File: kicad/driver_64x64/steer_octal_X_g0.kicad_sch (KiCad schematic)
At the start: 66 parts

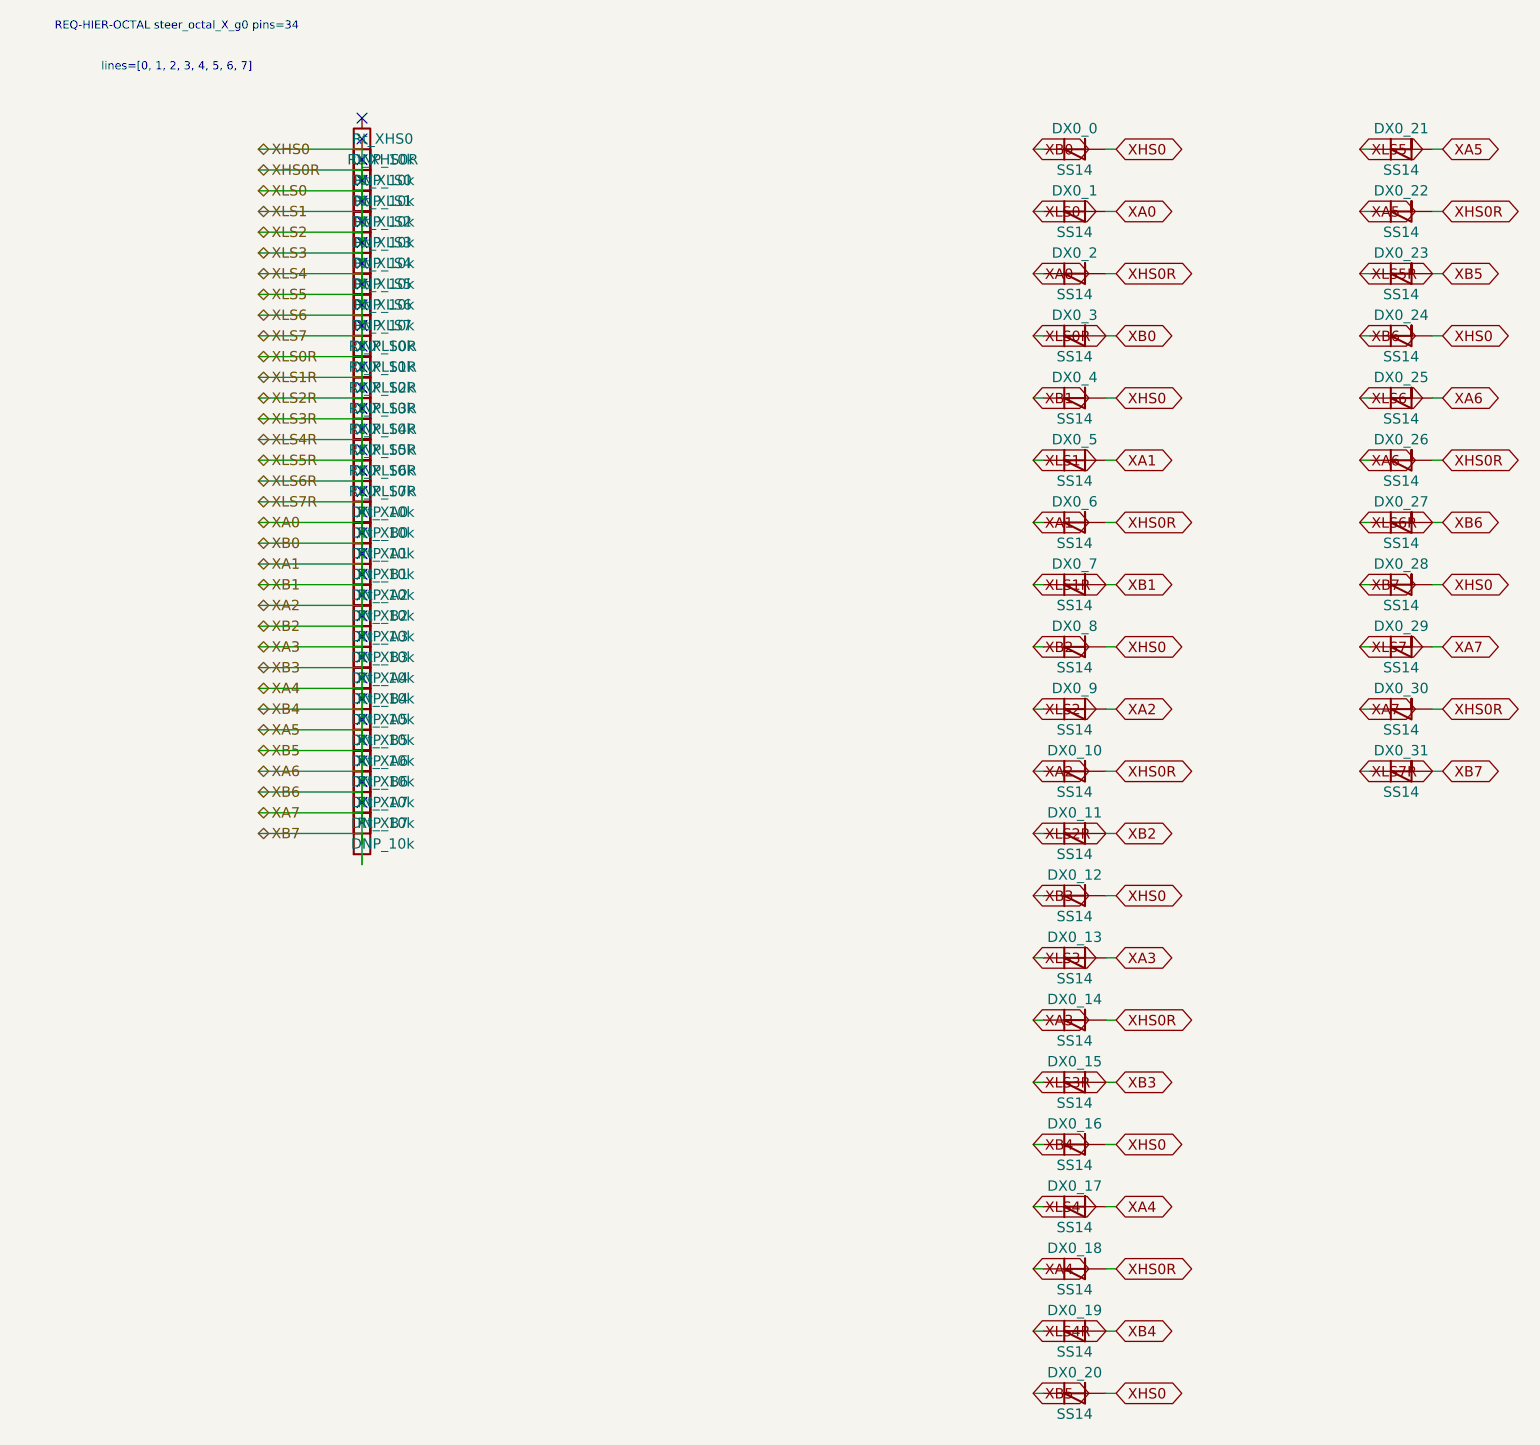
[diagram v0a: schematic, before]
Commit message: logical seperation into host and multiple decode/drive/steering boards
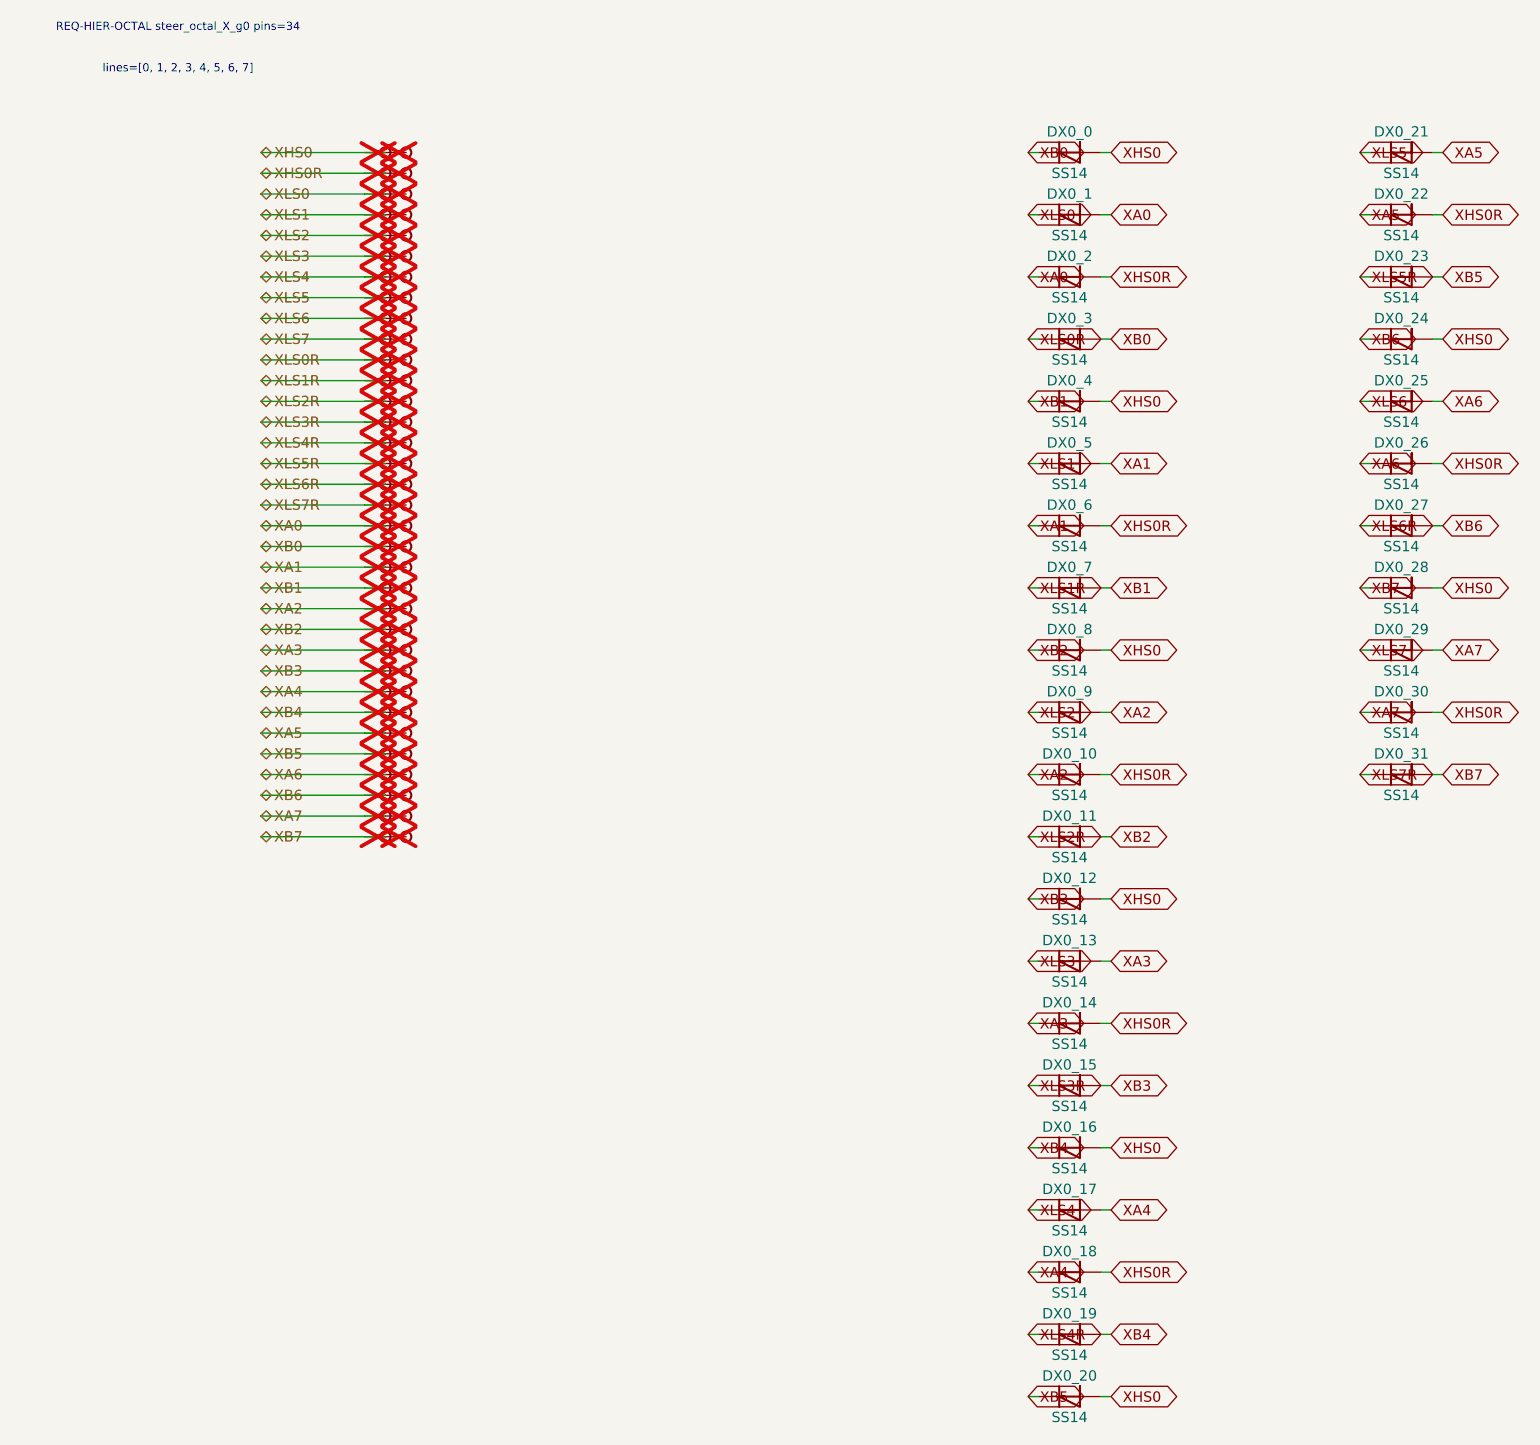
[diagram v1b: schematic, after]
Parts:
- removed Rt_XA0, Rt_XA1, Rt_XA2, Rt_XA3, Rt_XA4, Rt_XA5, Rt_XA6, Rt_XA7, Rt_XB0, Rt_XB1, Rt_XB2, Rt_XB3, Rt_XB4, Rt_XB5, Rt_XB6, Rt_XB7, Rt_XHS0, Rt_XHS0R, Rt_XLS0, Rt_XLS0R, Rt_XLS1, Rt_XLS1R, Rt_XLS2, Rt_XLS2R, Rt_XLS3, Rt_XLS3R, Rt_XLS4, Rt_XLS4R, Rt_XLS5, Rt_XLS5R, Rt_XLS6, Rt_XLS6R, Rt_XLS7, Rt_XLS7R: DNP_10k, symbol Device:R
- added TP_XA0, TP_XA0b, TP_XA1, TP_XA1b, TP_XA2, TP_XA2b, TP_XA3, TP_XA3b, TP_XA4, TP_XA4b, TP_XA5, TP_XA5b, TP_XA6, TP_XA6b, TP_XA7, TP_XA7b, TP_XB0, TP_XB0b, TP_XB1, TP_XB1b, TP_XB2, TP_XB2b, TP_XB3, TP_XB3b, TP_XB4, TP_XB4b, TP_XB5, TP_XB5b, TP_XB6, TP_XB6b, TP_XB7, TP_XB7b, TP_XHS0, TP_XHS0R, TP_XHS0Rb, TP_XHS0b, TP_XLS0, TP_XLS0R, TP_XLS0Rb, TP_XLS0b, TP_XLS1, TP_XLS1R, TP_XLS1Rb, TP_XLS1b, TP_XLS2, TP_XLS2R, TP_XLS2Rb, TP_XLS2b, TP_XLS3, TP_XLS3R, TP_XLS3Rb, TP_XLS3b, TP_XLS4, TP_XLS4R, TP_XLS4Rb, TP_XLS4b, TP_XLS5, TP_XLS5R, TP_XLS5Rb, TP_XLS5b, TP_XLS6, TP_XLS6R, TP_XLS6Rb, TP_XLS6b, TP_XLS7, TP_XLS7R, TP_XLS7Rb, TP_XLS7b: Stub, symbol CMR:Stub
- DX0_0, DX0_1, DX0_10, DX0_11, DX0_12, DX0_13, DX0_14, DX0_15, DX0_16, DX0_17, DX0_18, DX0_19, DX0_2, DX0_20, DX0_21, DX0_22, DX0_23, DX0_24, DX0_25, DX0_26, DX0_27, DX0_28, DX0_29, DX0_3, DX0_30, DX0_31, DX0_4, DX0_5, DX0_6, DX0_7, DX0_8, DX0_9: symbol Device:D_Schottky -> CMR:D_Schottky
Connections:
- net XA0: now also TP_XA0.1, TP_XA0b.1; no longer DX0_0.1 (K), DX0_0.2 (A), DX0_1.1 (K), DX0_10.1 (K), DX0_10.2 (A), DX0_11.1 (K), DX0_11.2 (A), DX0_12.1 (K), DX0_12.2 (A), DX0_13.1 (K), DX0_13.2 (A), DX0_14.1 (K), DX0_14.2 (A), DX0_15.1 (K), DX0_15.2 (A), DX0_16.1 (K), DX0_16.2 (A), DX0_17.1 (K), DX0_17.2 (A), DX0_18.1 (K), DX0_18.2 (A), DX0_19.1 (K), DX0_19.2 (A), DX0_2.2 (A), DX0_20.1 (K), DX0_20.2 (A), DX0_21.1 (K), DX0_21.2 (A), DX0_22.1 (K), DX0_22.2 (A), DX0_23.1 (K), DX0_23.2 (A), DX0_24.1 (K), DX0_24.2 (A), DX0_25.1 (K), DX0_25.2 (A), DX0_26.1 (K), DX0_26.2 (A), DX0_27.1 (K), DX0_27.2 (A), DX0_28.1 (K), DX0_28.2 (A), DX0_29.1 (K), DX0_29.2 (A), DX0_3.1 (K), DX0_3.2 (A), DX0_30.1 (K), DX0_30.2 (A), DX0_31.1 (K), DX0_31.2 (A), DX0_4.1 (K), DX0_4.2 (A), DX0_5.1 (K), DX0_5.2 (A), DX0_6.1 (K), DX0_6.2 (A), DX0_7.1 (K), DX0_7.2 (A), DX0_8.1 (K), DX0_8.2 (A), DX0_9.1 (K), DX0_9.2 (A)
- new net XA1: DX0_5.2 (A), DX0_6.1 (K), TP_XA1.1, TP_XA1b.1
- new net XA2: DX0_10.1 (K), DX0_9.2 (A), TP_XA2.1, TP_XA2b.1
- new net XA3: DX0_13.2 (A), DX0_14.1 (K), TP_XA3.1, TP_XA3b.1
- new net XA4: DX0_17.2 (A), DX0_18.1 (K), TP_XA4.1, TP_XA4b.1
- new net XA5: DX0_21.2 (A), DX0_22.1 (K), TP_XA5.1, TP_XA5b.1
- new net XA6: DX0_25.2 (A), DX0_26.1 (K), TP_XA6.1, TP_XA6b.1
- new net XA7: DX0_29.2 (A), DX0_30.1 (K), TP_XA7.1, TP_XA7b.1
- new net XB0: DX0_0.1 (K), DX0_3.2 (A), TP_XB0.1, TP_XB0b.1
- new net XB1: DX0_4.1 (K), DX0_7.2 (A), TP_XB1.1, TP_XB1b.1
- new net XB2: DX0_11.2 (A), DX0_8.1 (K), TP_XB2.1, TP_XB2b.1
- new net XB3: DX0_12.1 (K), DX0_15.2 (A), TP_XB3.1, TP_XB3b.1
- new net XB4: DX0_16.1 (K), DX0_19.2 (A), TP_XB4.1, TP_XB4b.1
- new net XB5: DX0_20.1 (K), DX0_23.2 (A), TP_XB5.1, TP_XB5b.1
- new net XB6: DX0_24.1 (K), DX0_27.2 (A), TP_XB6.1, TP_XB6b.1
- new net XB7: DX0_28.1 (K), DX0_31.2 (A), TP_XB7.1, TP_XB7b.1
- new net XHS0: DX0_0.2 (A), DX0_12.2 (A), DX0_16.2 (A), DX0_20.2 (A), DX0_24.2 (A), DX0_28.2 (A), DX0_4.2 (A), DX0_8.2 (A), TP_XHS0.1, TP_XHS0b.1
- new net XHS0R: DX0_10.2 (A), DX0_14.2 (A), DX0_18.2 (A), DX0_2.2 (A), DX0_22.2 (A), DX0_26.2 (A), DX0_30.2 (A), DX0_6.2 (A), TP_XHS0R.1, TP_XHS0Rb.1
- new net XLS0: DX0_1.1 (K), TP_XLS0.1, TP_XLS0b.1
- new net XLS0R: DX0_3.1 (K), TP_XLS0R.1, TP_XLS0Rb.1
- new net XLS1: DX0_5.1 (K), TP_XLS1.1, TP_XLS1b.1
- new net XLS1R: DX0_7.1 (K), TP_XLS1R.1, TP_XLS1Rb.1
- new net XLS2: DX0_9.1 (K), TP_XLS2.1, TP_XLS2b.1
- new net XLS2R: DX0_11.1 (K), TP_XLS2R.1, TP_XLS2Rb.1
- new net XLS3: DX0_13.1 (K), TP_XLS3.1, TP_XLS3b.1
- new net XLS3R: DX0_15.1 (K), TP_XLS3R.1, TP_XLS3Rb.1
- new net XLS4: DX0_17.1 (K), TP_XLS4.1, TP_XLS4b.1
- new net XLS4R: DX0_19.1 (K), TP_XLS4R.1, TP_XLS4Rb.1
- new net XLS5: DX0_21.1 (K), TP_XLS5.1, TP_XLS5b.1
- new net XLS5R: DX0_23.1 (K), TP_XLS5R.1, TP_XLS5Rb.1
- new net XLS6: DX0_25.1 (K), TP_XLS6.1, TP_XLS6b.1
- new net XLS6R: DX0_27.1 (K), TP_XLS6R.1, TP_XLS6Rb.1
- new net XLS7: DX0_29.1 (K), TP_XLS7.1, TP_XLS7b.1
- new net XLS7R: DX0_31.1 (K), TP_XLS7R.1, TP_XLS7Rb.1
- no-connect marks 34 -> 0
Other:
- moved on the sheet: DX0_0, DX0_1, DX0_10, DX0_11, DX0_12, DX0_13, DX0_14, DX0_15, DX0_16, DX0_17, DX0_18, DX0_19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
